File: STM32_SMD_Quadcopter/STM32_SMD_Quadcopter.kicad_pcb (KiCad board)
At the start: 2 copper layers, 36.5 x 25.4 mm, 61 parts, among them J1 PWR, J2 USB_B_Micro, J3 Micro_SD_Card_Det, J4 DEBUG, J5 DSMX, M1 Brushed_DC, M2 Brushed_DC, M3 Brushed_DC, M4 Brushed_DC, Q1 IRLML6244TR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

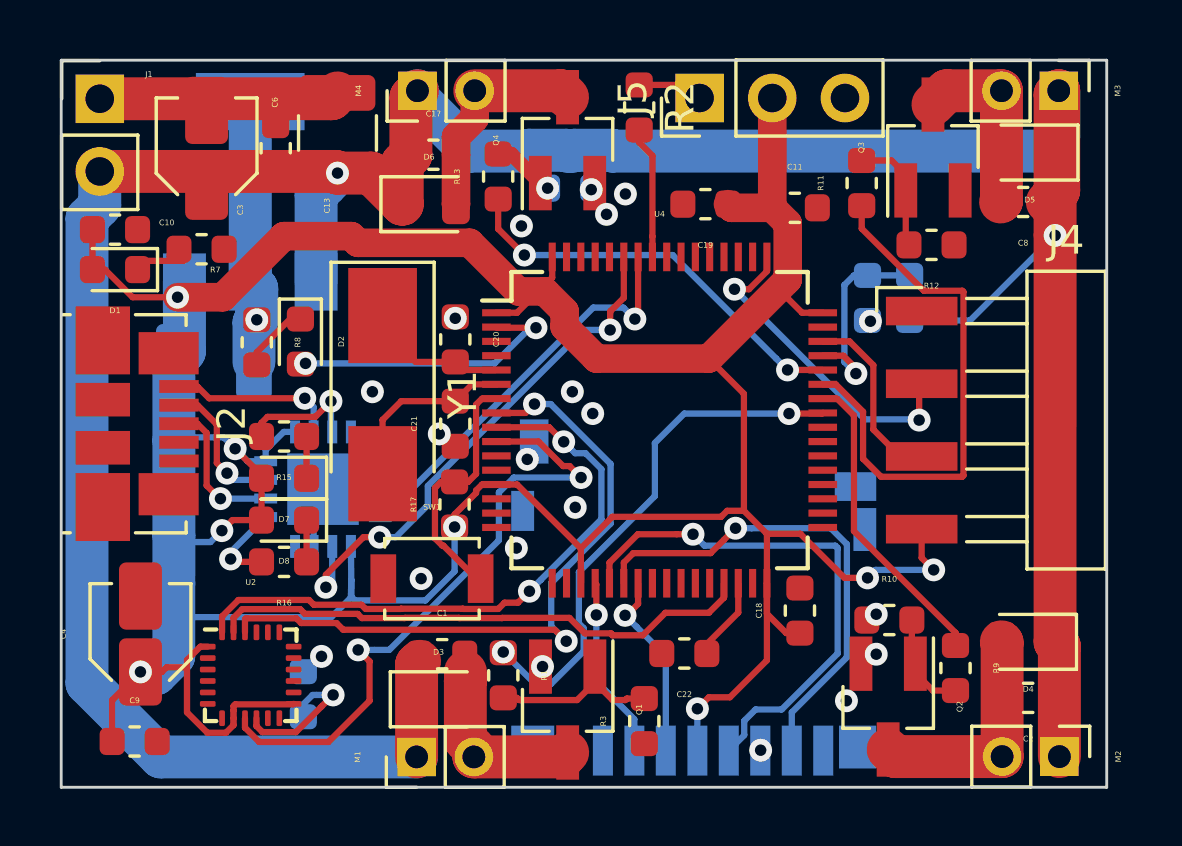
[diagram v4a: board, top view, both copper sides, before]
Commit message: fixed silkscreen
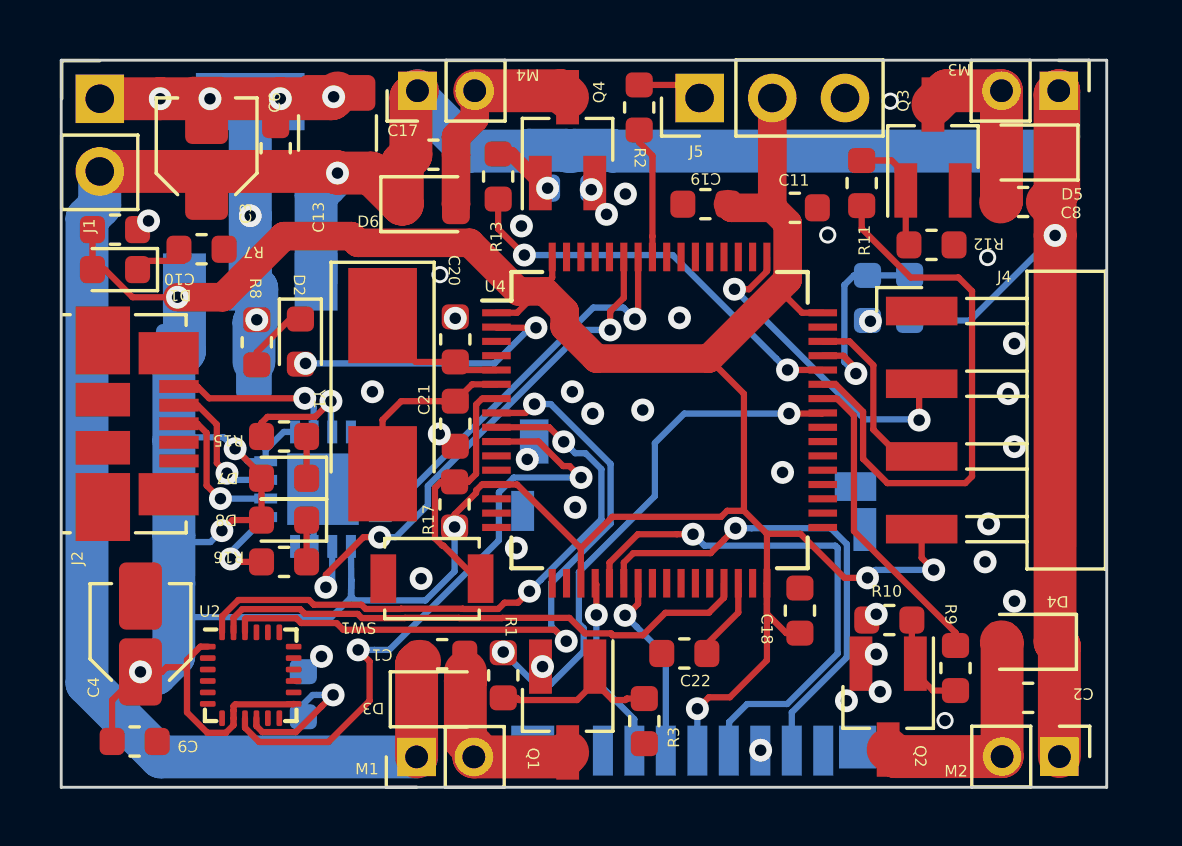
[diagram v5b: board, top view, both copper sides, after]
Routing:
- net MOTOR_C: track 18.9 -> 19.7 mm
- net GND: vias 21 -> 42

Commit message: Finished gerbers
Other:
- board text added: "Michael Langford Micro FCU V0.0"
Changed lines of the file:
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@@
   (general
     (thickness 1.6)
-    (drawings 4)
+    (drawings 5)
     (tracks 588)
     (zones 0)
@@
     (0 F.Cu signal)
     (31 B.Cu signal)
-    (32 B.Adhes user)
-    (33 F.Adhes user)
-    (34 B.Paste user)
-    (35 F.Paste user)
-    (36 B.SilkS user)
-    (37 F.SilkS user)
-    (38 B.Mask user)
-    (39 F.Mask user)
+    (32 B.Adhes user hide)
+    (33 F.Adhes user hide)
+    (34 B.Paste user hide)
+    (35 F.Paste user hide)
+    (36 B.SilkS user hide)
+    (37 F.SilkS user hide)
+    (38 B.Mask user hide)
+    (39 F.Mask user hide)
     (40 Dwgs.User user)
     (41 Cmts.User user)
@@
     (visible_elements 7FFDFFFF)
     (pcbplotparams
-      (layerselection 0x010fc_ffffffff)
+      (layerselection 0x010ff_ffffffff)
       (usegerberextensions false)
       (usegerberattributes false)
@@
       (drillshape 0)
       (scaleselection 1)
-      (outputdirectory "./Gerbers1"))
+      (outputdirectory "./Gerbers2"))
   )
   (net 0 "")
@@
     (tags resistor)
     (attr smd)
-    (fp_text reference R3 (at -0.56896 1.03124 90 unlocked) (layer F.SilkS)
+    (fp_text reference R3 (at 0.46482 1.15316 90 unlocked) (layer F.SilkS)
       (effects (font (size 0.4 0.4) (thickness 0.05)))
     )
@@
     )
   )
+  (gr_text "Michael Langford\nMicro FCU V0.0" (at 72.8726 52.2224) (layer F.SilkS)
+    (effects (font (size 0.508 0.508) (thickness 0.03175)))
+  )
   (gr_line (start 47.9044 53.3654) (end 47.9044 27.9654) (layer Edge.Cuts) (width 0.1))
   (gr_line (start 84.4296 53.3654) (end 47.9044 53.3654) (layer Edge.Cuts) (width 0.1))
   (gr_line (start 84.4296 27.9654) (end 84.4296 53.3654) (layer Edge.Cuts) (width 0.1))
   (gr_line (start 47.9044 27.9654) (end 84.4296 27.9654) (layer Edge.Cuts) (width 0.1))
-  (via (at 50.95494 33.5788) (size 0.8) (drill 0.4) (layers F.Cu B.Cu) (net 41))
   (segment (start 62.02259 49.630996) (end 62.026608 49.626978) (width 1.5) (layer F.Cu) (net 1) (status 30))
   (segment (start 62.026608 49.626978) (end 62.026608 49.331766) (width 1.5) (layer F.Cu) (net 1) (status 10))
@@
   (segment (start 49.6823 50.3259) (end 50.673 49.3352) (width 0.22) (layer F.Cu) (net 40))
   (segment (start 49.6823 51.7652) (end 49.6823 50.3259) (width 0.22) (layer F.Cu) (net 40))
+  (via (at 50.95494 33.5788) (size 0.8) (drill 0.4) (layers F.Cu B.Cu) (net 41))
   (via (at 76.3778 47.3202) (size 0.8) (drill 0.4) (layers F.Cu B.Cu) (net 41))
   (via (at 76.1746 37.084) (size 0.8) (drill 0.4) (layers F.Cu B.Cu) (net 41))

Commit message: All parts set in place
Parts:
- removed C11: 100nF, Capacitor_SMD:C_0603_1608Metric
- removed C13: 100uF, Capacitor_SMD:C_1210_3225Metric
- removed C4: 100uF, Capacitor_SMD:C_Elec_3x5.4
- added C16: 100nF, Capacitor_SMD:C_0402_1005Metric, F.Cu at (78.6, 48.2)
- added Q5: 2N7002, Package_TO_SOT_SMD:SOT-23, B.Cu at (81.0, 43.2)
- added R18: 1K, Resistor_SMD:R_0402_1005Metric, F.Cu at (81.1, 46.4)
- added R19: 1.2K, Resistor_SMD:R_0402_1005Metric, F.Cu at (81.1, 43.4)
- added R20: 1K, Resistor_SMD:R_0402_1005Metric, F.Cu at (79.2, 45.4)
- added R21: 10K, Resistor_SMD:R_0402_1005Metric, F.Cu at (79.2, 46.4)
- added R22: 1K, Resistor_SMD:R_0402_1005Metric, F.Cu at (81.1, 45.4)
- added R23: 1.2K, Resistor_SMD:R_0402_1005Metric, F.Cu at (81.1, 44.4)
- added R24: 1.2K, Resistor_SMD:R_0402_1005Metric, F.Cu at (79.2, 44.4)
- added R25: 22, Resistor_SMD:R_0402_1005Metric, F.Cu at (54.2, 44.2)
- added R6: 10K, Resistor_SMD:R_0402_1005Metric, F.Cu at (79.2, 43.4)
- added U5: ICM-20948, Sensor_Motion:InvenSense_QFN-24_3x3mm_P0.4mm, B.Cu at (81.2, 49.3)
- C1, C10, C17, C2, C8, C9: footprint Capacitor_SMD:C_0603_1608Metric -> Capacitor_SMD:C_0402_1005Metric
- C20, C21: value 22pF -> 12pF
- C7: footprint Capacitor_SMD:C_0603_1608Metric -> Capacitor_SMD:C_0402_1005Metric; moved to F.Cu
- J4: footprint STM32_SMD_Quadcopter:Harwin_M20-89004xx_1x04_P2.54mm_Horizontal_MODIFIEDSILKSCREEN -> Connector_PinSocket_1.27mm:PinSocket_2x05_P1.27mm_Vertical_SMD
- Q1, Q2, Q3, Q4: moved to B.Cu
- R14, U3: moved to F.Cu
- R15, R16: value 300 -> 2K
- R4: value 3K -> 30K; moved to F.Cu
- R5: value 10K -> 100K; moved to F.Cu
- R7, R8: value 470 -> 4.7k
- U1: value LT1129-3.3_SOT223 -> AMS1117-3.3
- U2: value MPU-9250 -> AMS1117-1.8; footprint Sensor_Motion:InvenSense_QFN-24_3x3mm_P0.4mm -> Package_TO_SOT_SMD:SOT-223-3_TabPin2; moved to B.Cu
- Y1: value 8MHz ECS801830JGNTR -> 16MHz X322516MLB4SI; footprint Crystal:Crystal_SMD_Abracon_ABM3-2Pin_5.0x3.2mm_HandSoldering -> Crystal:Crystal_SMD_3225-4Pin_3.2x2.5mm
- moved U2 28.1 mm to (79.3, 36.3)
- moved C7 26.4 mm to (82.7, 48.3), turned to 270 degrees
- moved R17 22.4 mm to (83.8, 40.0)
- moved R9 21.1 mm to (58.2, 51.7)
- moved D4 21.1 mm to (60.6, 49.3)
- moved SW1 20.7 mm to (80.6, 40.0)
- moved R10 20.5 mm to (56.7, 51.7), turned to 270 degrees
- moved M2 20.3 mm to (62.5, 51.7)
- moved Q2 19.2 mm to (57.6, 50.5), turned to 90 degrees
- moved C2 18.9 mm to (62.8, 49.3), turned to 90 degrees
- moved R4 18.0 mm to (65.2, 49.4), turned to 0 degrees
- moved R5 15.3 mm to (68.2, 49.4), turned to 0 degrees
- moved R12 13.1 mm to (66.2, 29.5), turned to 90 degrees
- moved R3 13.0 mm to (55.2, 51.7), turned to 270 degrees
- moved C10 12.2 mm to (56.2, 44.2)
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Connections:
- C10 pad 2: +3V3 -> Net-(C10-Pad2)
- C20 pad 1: GND -> Net-(C20-Pad1)
- C20 pad 2: Net-(C20-Pad2) -> GND
- C21 pad 1: GND -> Net-(C21-Pad1)
- C21 pad 2: Net-(C21-Pad2) -> GND
- J4 pad 1: GND -> +3V3
- J4 pad 2: SYS_JTCL-SWCLK -> SYS_JTMS-SWDIO
- J4 pad 3: SYS_JTMS-SWDIO -> GND
- J4 pad 4: +3V3 -> SYS_JTCL-SWCLK
- R17 pad 2: Net-(R17-Pad2) -> NRST
- SW1 pad 2: Net-(R17-Pad2) -> NRST
- U1 pad 1: +BATT -> GND
- U1 pad 2: GND -> +3V3
- U1 pad 3: +3V3 -> +BATT
- U2 pad 1: +3V3 -> GND
- U2 pad 2: (no net) -> +1V8
- U2 pad 3: (no net) -> +3V3
- U3 pad 8: +3V3 -> Net-(C10-Pad2)
- U3 pad 9: +3V3 -> Net-(C10-Pad2)
- U4 pad 5: Net-(C20-Pad2) -> Net-(C20-Pad1)
- U4 pad 6: Net-(C21-Pad2) -> Net-(C21-Pad1)
- U4 pad 7: Net-(R17-Pad2) -> NRST
- Y1 pad 1: Net-(C20-Pad2) -> Net-(C20-Pad1)
- Y1 pad 2: Net-(C21-Pad2) -> GND
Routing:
- net +3V3: track 137.8 -> 0.00 mm, vias 8 -> 0
- net +BATT: track 112.4 -> 0.00 mm, vias 2 -> 0
- net MPU9250_CS: track 24.3 -> 0.00 mm, vias 2 -> 0
- net SPI2_MISO: track 22.2 -> 0.00 mm, vias 2 -> 0
- net GND: track 22.2 -> 0.00 mm, vias 42 -> 0
- net SPI2_MOSI: track 21.5 -> 0.00 mm, vias 2 -> 0
- net MOTOR_C: track 19.7 -> 0.00 mm
- net SPI2_SCK: track 19.2 -> 0.00 mm
- net SPI1_SCK: track 18.8 -> 0.00 mm, vias 1 -> 0
- net USART1_RX: track 18.6 -> 0.00 mm, vias 3 -> 0
- net MOTOR_A: track 18.5 -> 0.00 mm, vias 2 -> 0
- net SPI1_MISO: track 17.2 -> 0.00 mm, vias 1 -> 0
- net MOTOR_D: track 14.4 -> 0.00 mm, vias 2 -> 0
- net USART1_TX: track 14.0 -> 0.00 mm, vias 1 -> 0
- net SYS_JTCL-SWCLK: track 11.5 -> 0.00 mm, vias 2 -> 0
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
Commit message: completed switchover to MPU6050
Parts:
- removed C16: 100nF, Capacitor_SMD:C_0402_1005Metric
- removed Q5: 2N7002, Package_TO_SOT_SMD:SOT-23
- removed R19, R23, R24: 1.2K, Resistor_SMD:R_0402_1005Metric
- removed R20, R22: 1K, Resistor_SMD:R_0402_1005Metric
- removed R21: 10K, Resistor_SMD:R_0402_1005Metric
- removed U2: AMS1117-1.8, Package_TO_SOT_SMD:SOT-223-3_TabPin2
- added C11: 0.1uF 2V, Capacitor_SMD:C_0402_1005Metric, F.Cu at (80.6, 51.3)
- added C12: 2.2nF, 50V, Capacitor_SMD:C_0805_2012Metric, F.Cu at (81.6, 44.9)
- added C4: 10nF, 4V, Capacitor_SMD:C_0402_1005Metric, F.Cu at (78.8, 51.4)
- C7: value 0.1uF -> 0.1uF 4V
- R18: value 1K -> 4.7K; footprint Resistor_SMD:R_0402_1005Metric -> Resistor_SMD:R_0603_1608Metric
- R6: value 10K -> 4.7K; footprint Resistor_SMD:R_0402_1005Metric -> Resistor_SMD:R_0603_1608Metric
- U5: value ICM-20948 -> MPU-6050; footprint Sensor_Motion:InvenSense_QFN-24_3x3mm_P0.4mm -> Sensor_Motion:InvenSense_QFN-24_4x4mm_P0.5mm; moved to F.Cu
- moved C5 5.10 mm to (57.9, 40.7), turned to 270 degrees
- moved C2 4.87 mm to (58.0, 48.4), turned to 270 degrees
- moved C1 4.71 mm to (53.7, 48.4), turned to 270 degrees
- moved C9 4.63 mm to (65.2, 49.1), turned to 180 degrees
- moved C17 4.46 mm to (63.1, 32.0), turned to 90 degrees
- moved R18 3.15 mm to (78.3, 45.0)
- moved R7 3.12 mm to (49.5, 35.5)
- moved C7 3.08 mm to (82.5, 51.3), turned to 180 degrees
- moved R4 2.93 mm to (65.1, 52.3)
- moved R5 2.93 mm to (68.1, 52.3)
- moved U1 2.41 mm to (54.8, 34.9), turned to 0 degrees
- moved C22 2.28 mm to (71.6, 48.0), turned to 0 degrees
- moved M3 2.15 mm to (69.7, 29.5), turned to 90 degrees
- moved R8 1.32 mm to (58.3, 35.6), turned to 90 degrees
- moved D1 1.27 mm to (49.5, 34.0), turned to 0 degrees
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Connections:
- C7 pad 1: Net-(C7-Pad1) -> +3V3
- J4 pad 6: (no net) -> SYS_JTCL-SWO
- R18 pad 1: SPI2_MOSI -> +3V3
- R18 pad 2: SPI2_MOSI_1.8V -> I2C1_SDA
- R6 pad 1: +1V8 -> +3V3
- R6 pad 2: SPI2_MISO_1.8V -> I2C1_SCL
- U4 pad 10: SPI2_MISO -> (no net)
- U4 pad 29: SPI2_SCK -> (no net)
- U4 pad 41: MOTOR_A -> MOTOR_B
- U4 pad 42: MOTOR_B -> MOTOR_A
- U4 pad 43: MOTOR_C -> MOTOR_D
- U4 pad 44: MOTOR_D -> MOTOR_C
- U4 pad 55: (no net) -> SYS_JTCL-SWO
- U4 pad 61: (no net) -> I2C1_SCL
- U4 pad 62: (no net) -> I2C1_SDA
- U4 pad 8: MPU9250_CS -> (no net)
- U4 pad 9: SPI2_MOSI -> (no net)
- U5 pad 10: Net-(C7-Pad1) -> Net-(C11-Pad1)
- U5 pad 20: GND -> Net-(C12-Pad1)
- U5 pad 22: MPU9250_CS_1.8V -> (no net)
- U5 pad 23: SPI2_SCK_1.8V -> I2C1_SCL
- U5 pad 24: SPI2_MOSI_1.8V -> I2C1_SDA
- U5 pad 8: +1V8 -> +3V3
- U5 pad 9: SPI2_MISO_1.8V -> GND
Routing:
- net +3V3: track 0.00 -> 142.2 mm, vias 0 -> 21
- net +BATT: track 0.00 -> 77.0 mm, vias 0 -> 1
- net MOTOR_B: track 0.00 -> 31.6 mm, vias 0 -> 4
- net MOTOR_A: track 0.00 -> 31.5 mm, vias 0 -> 4
- net USART1_TX: track 0.00 -> 31.3 mm, vias 0 -> 4
- net NRST: track 0.00 -> 24.1 mm, vias 0 -> 2
- net VSENSE: track 0.00 -> 23.3 mm, vias 0 -> 2
- net I2C1_SCL: track 0.00 -> 22.3 mm, vias 0 -> 2
- net USART1_RX: track 0.00 -> 22.3 mm, vias 0 -> 2
- net I2C1_SDA: track 0.00 -> 21.8 mm, vias 0 -> 2
- net MOTOR_D: track 0.00 -> 15.6 mm, vias 0 -> 2
- net MOTOR_C: track 0.00 -> 14.5 mm, vias 0 -> 2
- net GND: track 0.00 -> 13.3 mm, vias 0 -> 37
- net SPI1_MISO: track 0.00 -> 11.3 mm, vias 0 -> 1
- net SYS_JTCL-SWO: track 0.00 -> 11.1 mm, vias 0 -> 2
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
